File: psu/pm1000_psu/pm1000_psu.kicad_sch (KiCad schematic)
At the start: 46 parts, among them J1 , J2 , J3 , J4 , J5 , U1 LM317_TO-220, U2 LM317_TO-220, U3 LM317_TO-220

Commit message: rework the psu layout a bit
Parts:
- R1, R2, R6: footprint Resistor_THT:R_Axial_DIN0414_L11.9mm_D4.5mm_P20.32mm_Horizontal -> Resistor_THT:R_Axial_DIN0411_L9.9mm_D3.6mm_P15.24mm_Horizontal
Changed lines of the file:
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@@
     (property "Reference" "R6" (id 0) (at 120.65 88.9 90))
     (property "Value" "1R 1W" (id 1) (at 120.65 91.44 90))
-    (property "Footprint" "Resistor_THT:R_Axial_DIN0414_L11.9mm_D4.5mm_P20.32mm_Horizontal" (id 2) (at 120.65 93.98 0)
+    (property "Footprint" "Resistor_THT:R_Axial_DIN0411_L9.9mm_D3.6mm_P15.24mm_Horizontal" (id 2) (at 120.65 93.98 0)
       (effects (font (size 1.27 1.27)) hide)
     )
@@
     (property "Reference" "R2" (id 0) (at 130.81 33.02 90))
     (property "Value" "1R 1W" (id 1) (at 130.81 35.56 90))
-    (property "Footprint" "Resistor_THT:R_Axial_DIN0414_L11.9mm_D4.5mm_P20.32mm_Horizontal" (id 2) (at 130.81 38.1 0)
+    (property "Footprint" "Resistor_THT:R_Axial_DIN0411_L9.9mm_D3.6mm_P15.24mm_Horizontal" (id 2) (at 130.81 38.1 0)
       (effects (font (size 1.27 1.27)) hide)
     )
@@
     (property "Reference" "R1" (id 0) (at 120.65 33.02 90))
     (property "Value" "1R 1W" (id 1) (at 120.65 35.56 90))
-    (property "Footprint" "Resistor_THT:R_Axial_DIN0414_L11.9mm_D4.5mm_P20.32mm_Horizontal" (id 2) (at 120.65 38.1 0)
+    (property "Footprint" "Resistor_THT:R_Axial_DIN0411_L9.9mm_D3.6mm_P15.24mm_Horizontal" (id 2) (at 120.65 38.1 0)
       (effects (font (size 1.27 1.27)) hide)
     )
@@
     )
     (path "/bf44974b-43bc-4ff5-8f96-747697bd08a6"
-      (reference "R1") (unit 1) (value "1R 1W") (footprint "Resistor_THT:R_Axial_DIN0414_L11.9mm_D4.5mm_P20.32mm_Horizontal")
+      (reference "R1") (unit 1) (value "1R 1W") (footprint "Resistor_THT:R_Axial_DIN0411_L9.9mm_D3.6mm_P15.24mm_Horizontal")
     )
     (path "/6206e7d6-1501-496d-8722-8b1c0a17018a"
-      (reference "R2") (unit 1) (value "1R 1W") (footprint "Resistor_THT:R_Axial_DIN0414_L11.9mm_D4.5mm_P20.32mm_Horizontal")
+      (reference "R2") (unit 1) (value "1R 1W") (footprint "Resistor_THT:R_Axial_DIN0411_L9.9mm_D3.6mm_P15.24mm_Horizontal")
     )
     (path "/a016d1a8-57d0-439d-9a40-a707ee777b0b"
@@
     )
     (path "/4655e229-4892-4a2f-b152-1c6ad26f2c21"
-      (reference "R6") (unit 1) (value "1R 1W") (footprint "Resistor_THT:R_Axial_DIN0414_L11.9mm_D4.5mm_P20.32mm_Horizontal")
+      (reference "R6") (unit 1) (value "1R 1W") (footprint "Resistor_THT:R_Axial_DIN0411_L9.9mm_D3.6mm_P15.24mm_Horizontal")
     )
     (path "/42c9cd22-ac7d-4ed1-85a6-b96816db1f7d"

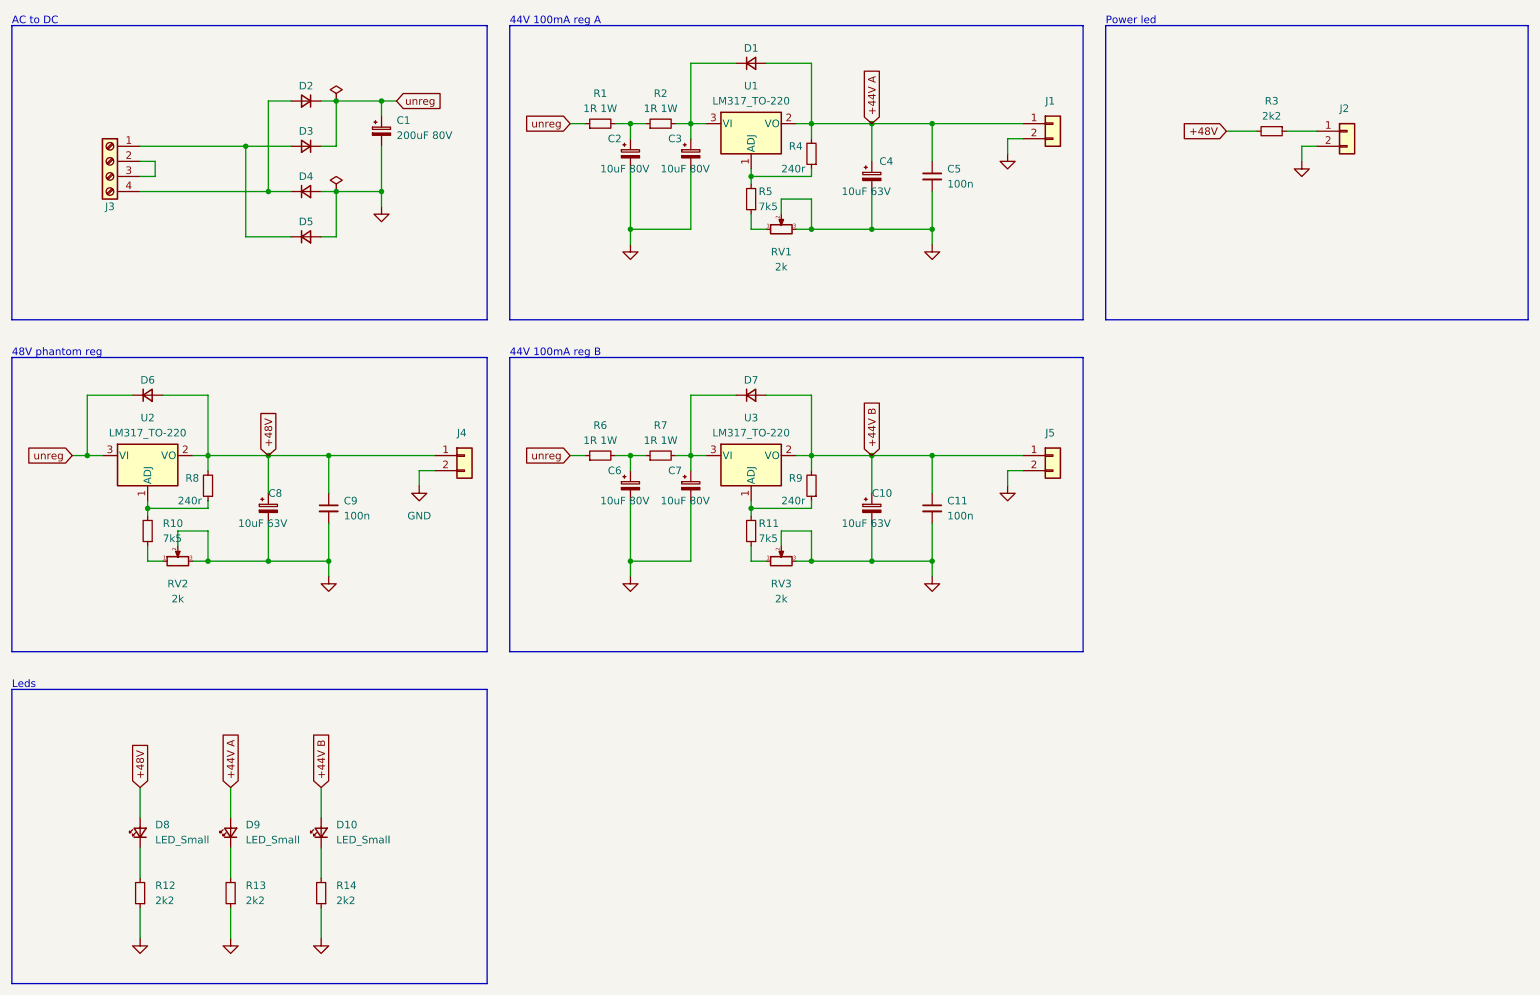
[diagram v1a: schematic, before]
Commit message: simplify filter stages for 44v channels
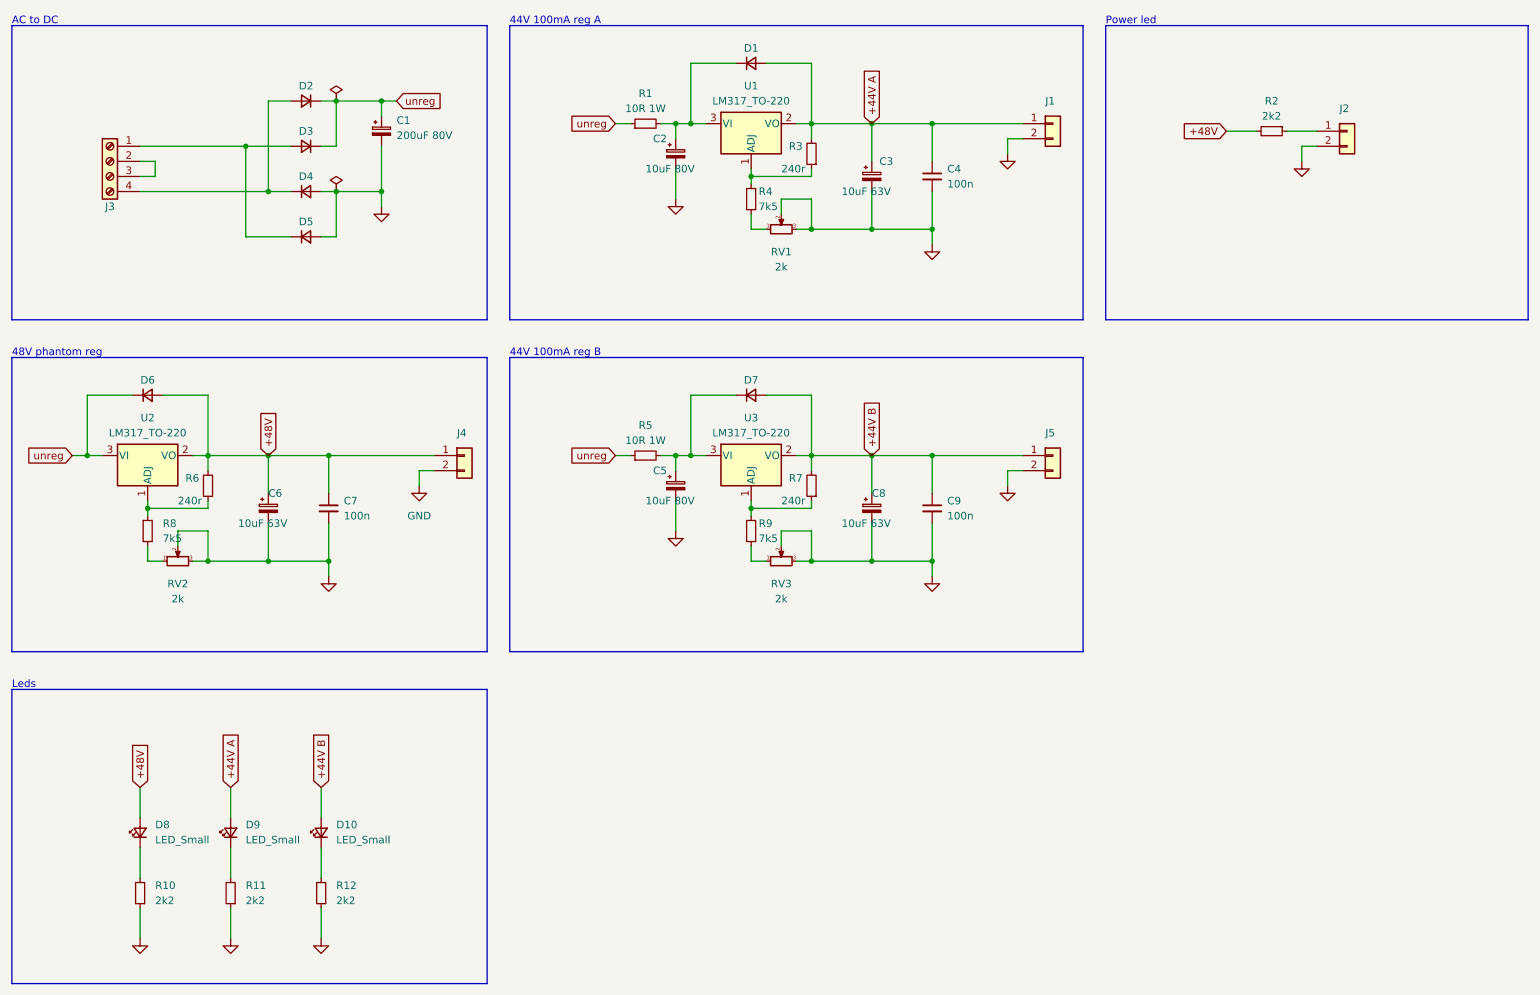
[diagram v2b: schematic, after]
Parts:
- removed C3, C7: 10uF 80V, Capacitor_THT:CP_Radial_D6.3mm_P2.50mm, symbol Device:C_Polarized_Small
- removed R2: 1R 1W, Resistor_THT:R_Axial_DIN0411_L9.9mm_D3.6mm_P15.24mm_Horizontal, symbol Device:R_Small
- removed R7: 1R 1W, Resistor_THT:R_Axial_DIN0414_L11.9mm_D4.5mm_P20.32mm_Horizontal, symbol Device:R_Small
- R1: value 1R 1W -> 10R 1W
- R5: renamed from R6; value 1R 1W -> 10R 1W
- renumbered C4 to C3, C5 to C4, C6 to C5, C8 to C6, C9 to C7, C10 to C8, C11 to C9, R12 to R10, R13 to R11, R14 to R12, R3 to R2, R4 to R3, R5 to R4, R8 to R6, R9 to R7, R10 to R8, R11 to R9
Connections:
- net at C2.1, R1.2: now also D1.1 (K), U1.3 (VI)
- net at D7.1 (K), U3.3 (VI): now also C5.1, R5.2
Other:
- moved on the sheet: C2, C5, R1, R5

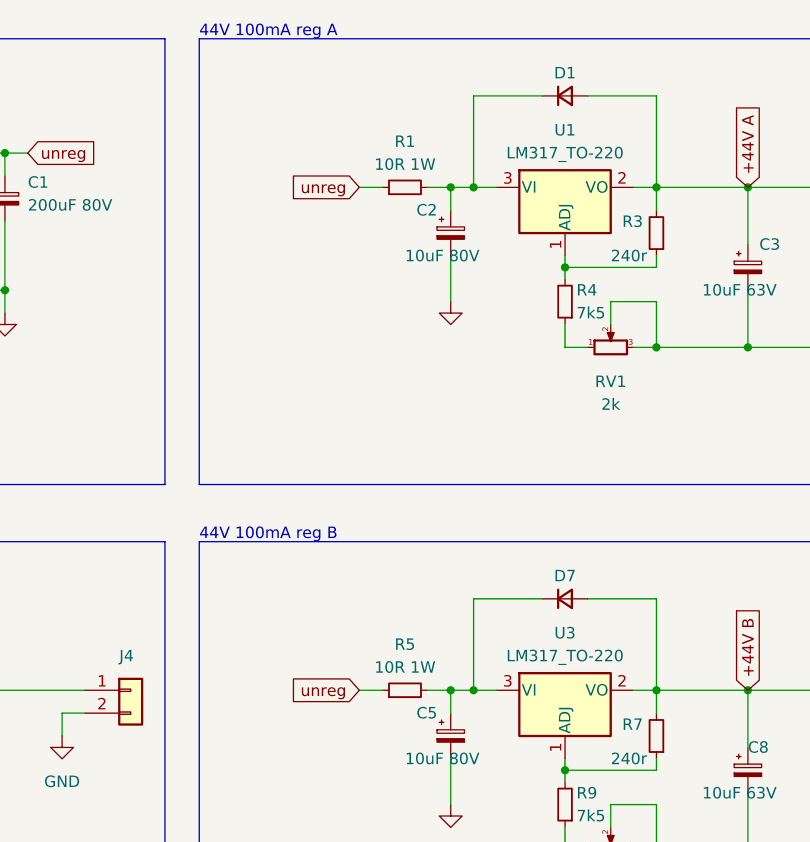
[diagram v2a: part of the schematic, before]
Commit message: increase pre reg filter r to 100ohm to accomodate for the lower current
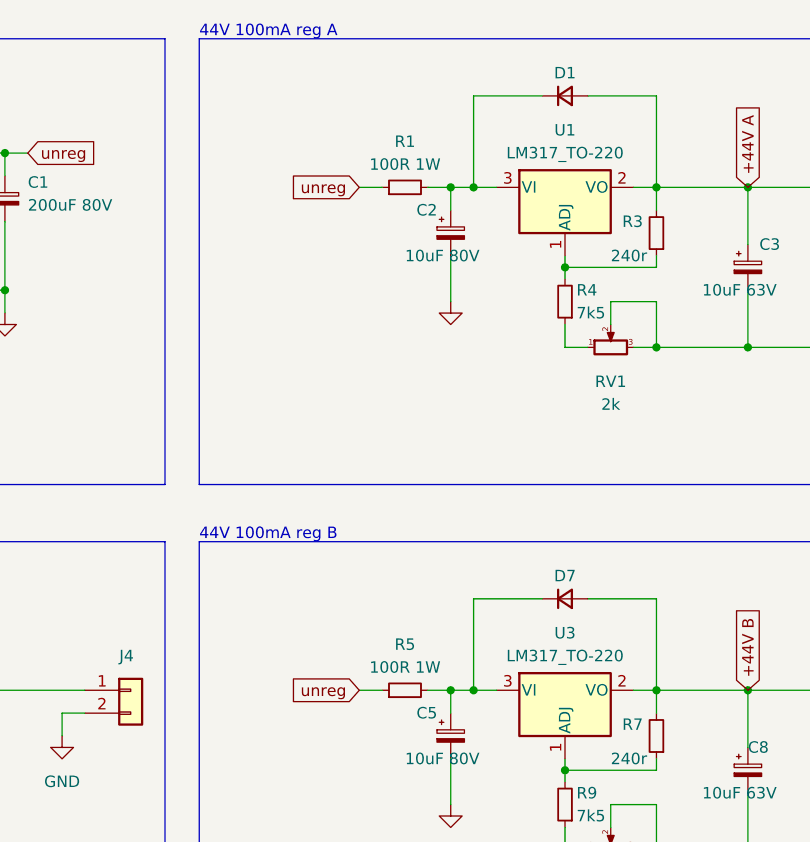
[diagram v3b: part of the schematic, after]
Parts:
- R1, R5: value 10R 1W -> 100R 1W
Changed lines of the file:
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@@
     (in_bom yes) (on_board yes)
     (property "Reference" "R5" (id 0) (at 128.27 88.9 90))
-    (property "Value" "10R 1W" (id 1) (at 128.27 91.44 90))
+    (property "Value" "100R 1W" (id 1) (at 128.27 91.44 90))
     (property "Footprint" "Resistor_THT:R_Axial_DIN0411_L9.9mm_D3.6mm_P15.24mm_Horizontal" (id 2) (at 128.27 93.98 0)
       (effects (font (size 1.27 1.27)) hide)
@@
     (in_bom yes) (on_board yes)
     (property "Reference" "R1" (id 0) (at 128.27 33.02 90))
-    (property "Value" "10R 1W" (id 1) (at 128.27 35.56 90))
+    (property "Value" "100R 1W" (id 1) (at 128.27 35.56 90))
     (property "Footprint" "Resistor_THT:R_Axial_DIN0411_L9.9mm_D3.6mm_P15.24mm_Horizontal" (id 2) (at 128.27 38.1 0)
       (effects (font (size 1.27 1.27)) hide)
@@
     )
     (path "/bf44974b-43bc-4ff5-8f96-747697bd08a6"
-      (reference "R1") (unit 1) (value "10R 1W") (footprint "Resistor_THT:R_Axial_DIN0411_L9.9mm_D3.6mm_P15.24mm_Horizontal")
+      (reference "R1") (unit 1) (value "100R 1W") (footprint "Resistor_THT:R_Axial_DIN0411_L9.9mm_D3.6mm_P15.24mm_Horizontal")
     )
     (path "/a016d1a8-57d0-439d-9a40-a707ee777b0b"
@@
     )
     (path "/4655e229-4892-4a2f-b152-1c6ad26f2c21"
-      (reference "R5") (unit 1) (value "10R 1W") (footprint "Resistor_THT:R_Axial_DIN0411_L9.9mm_D3.6mm_P15.24mm_Horizontal")
+      (reference "R5") (unit 1) (value "100R 1W") (footprint "Resistor_THT:R_Axial_DIN0411_L9.9mm_D3.6mm_P15.24mm_Horizontal")
     )
     (path "/cb3b6d3e-a1de-42f4-9013-7a4ac90bd06f"

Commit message: new layout
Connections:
- net GND: now also R4.1, R8.1, R9.1; no longer RV1.2, RV1.3, RV2.2, RV2.3, RV3.2, RV3.3
- net at RV1.1: now also R3.1, RV1.2, U1.1 (ADJ); no longer R4.1
- net at R7.1, U3.1 (ADJ): now also RV3.1, RV3.2; no longer R9.2
- net at RV2.1: now also R6.1, RV2.2, U2.1 (ADJ); no longer R8.1
- new net: R4.2, RV1.3
- new net: R9.2, RV3.3
- new net: R8.2, RV2.3
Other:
- moved on the sheet: R4, R8, R9, RV1, RV2, RV3
